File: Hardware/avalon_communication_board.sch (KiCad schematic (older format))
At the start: 22 parts, among them IC1 ENC28J60-I/SO, J1 RJ45_LEDS, P1 B2P-VH, Q1 FMMT597, Q2 BC817, Q3 BC817, Q4 FMMT597, Q5 BC817

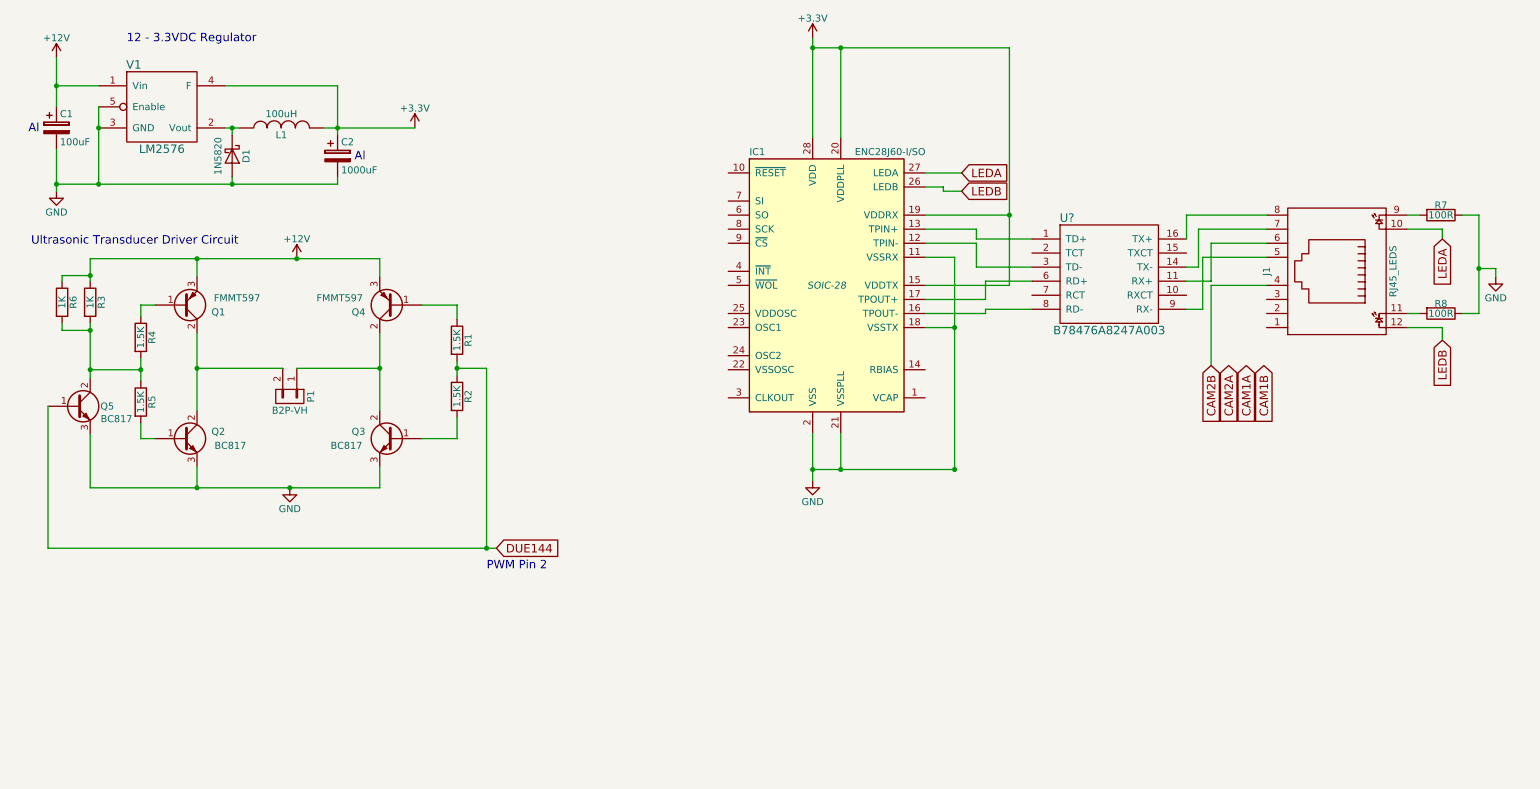
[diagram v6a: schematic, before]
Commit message: -Ethernet Controller Main Schematic Updated
-Main schematic almost complete with Pulse Transformers and Filtering
-Capacitors for Crystal Oscillator need adding
-Ethernet Controller schematic block added to main schematic sheet
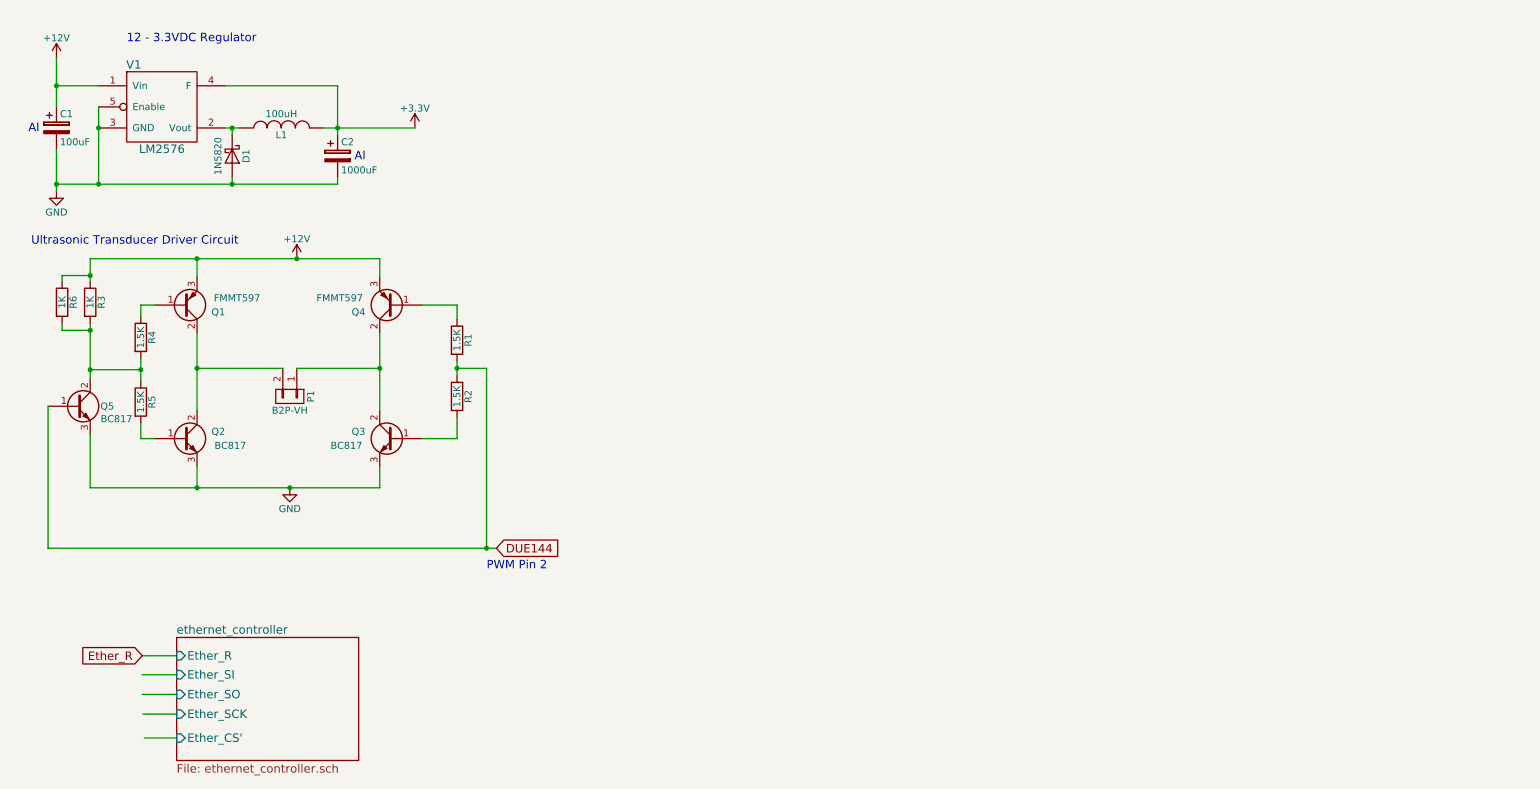
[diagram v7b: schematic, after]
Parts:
- removed IC1: ENC28J60-I/SO, SOIC-28, symbol ENC28J60-I/SO
- removed J1: RJ45_LEDS, symbol RJ45_LEDS
- removed R7, R8: 100R, symbol R
- removed U?: B78476A8247A003, symbol B78476A8247A003
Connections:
- net labels added: Ether_R
- net labels removed: CAM1A, CAM1B, CAM2A, CAM2B, LEDA, LEDB
- wire segments 96 -> 49
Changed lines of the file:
@@
 $Descr A4 11693 8268
 encoding utf-8
-Sheet 1 1
+Sheet 1 2
 Title ""
 Date ""
@@
 $EndComp
 $Comp
-L ENC28J60-I/SO IC1
-U 1 1 5A903E11
-P 6280 2470
-F 0 "IC1" H 5730 3420 50  0000 L CNN
-F 1 "ENC28J60-I/SO" H 6480 3420 50  0000 L CNN
-F 2 "SOIC-28" H 6280 2470 50  0000 C CIN
-F 3 "" H 6280 2470 50  0000 C CNN
-	1    6280 2470
-	1    0    0    -1
-$EndComp
-$Comp
-L RJ45_LEDS J1
-U 1 1 5A9063FA
-P 9910 2370
-F 0 "J1" H 9910 1870 50  0000 C CNN
-F 1 "RJ45_LEDS" H 9910 2770 50  0000 C CNN
-F 2 "" H 9910 2320 50  0000 C CNN
-F 3 "" H 9910 2320 50  0000 C CNN
-	1    9910 2370
-	0    1    -1   0
-$EndComp
-$Comp
 L +12V #PWR4
 U 1 1 5A907F46
@@
 $EndComp
 Connection ~ 2510 2280
-$Comp
-L +3.3V #PWR6
-U 1 1 5A908CDC
-P 6180 710
-F 0 "#PWR6" H 6180 560 50  0001 C CNN
-F 1 "+3.3V" H 6180 850 50  0000 C CNN
-F 2 "" H 6180 710 50  0000 C CNN
-F 3 "" H 6180 710 50  0000 C CNN
-	1    6180 710
-	1    0    0    -1
-$EndComp
-$Comp
-L GND #PWR7
-U 1 1 5A90B1AB
-P 6180 3860
-F 0 "#PWR7" H 6180 3610 50  0001 C CNN
-F 1 "GND" H 6180 3710 50  0000 C CNN
-F 2 "" H 6180 3860 50  0000 C CNN
-F 3 "" H 6180 3860 50  0000 C CNN
-	1    6180 3860
-	1    0    0    -1
-$EndComp
-Text GLabel 7240 1670 2    60   Input ~ 0
-LEDA
-Text GLabel 7240 1800 2    60   Input ~ 0
-LEDB
-$Comp
-L R R7
-U 1 1 5A911D20
-P 10650 1970
-F 0 "R7" V 10580 1970 50  0000 C CNN
-F 1 "100R" V 10650 1970 50  0000 C CNN
-F 2 "" V 10580 1970 50  0000 C CNN
-F 3 "" H 10650 1970 50  0000 C CNN
-	1    10650 1970
-	0    1    1    0
-$EndComp
-$Comp
-L R R8
-U 1 1 5A91211B
-P 10650 2670
-F 0 "R8" V 10580 2670 50  0000 C CNN
-F 1 "100R" V 10650 2670 50  0000 C CNN
-F 2 "" V 10580 2670 50  0000 C CNN
-F 3 "" H 10650 2670 50  0000 C CNN
-	1    10650 2670
-	0    1    1    0
-$EndComp
-Text GLabel 10660 2140 3    60   Input ~ 0
-LEDA
-$Comp
-L GND #PWR9
-U 1 1 5A913778
-P 11040 2410
-F 0 "#PWR9" H 11040 2160 50  0001 C CNN
-F 1 "GND" H 11040 2260 50  0000 C CNN
-F 2 "" H 11040 2410 50  0000 C CNN
-F 3 "" H 11040 2410 50  0000 C CNN
-	1    11040 2410
-	1    0    0    -1
-$EndComp
-Text GLabel 10660 2860 3    60   Input ~ 0
-LEDB
-Wire Wire Line
-	10410 2770 10660 2770
-Wire Wire Line
-	10660 2770 10660 2860
-Wire Wire Line
-	10920 2670 10800 2670
-Wire Wire Line
-	10800 1970 10920 1970
-Wire Wire Line
-	10920 1970 10920 2670
-Wire Wire Line
-	11040 2410 11040 2350
-Wire Wire Line
-	11040 2350 10920 2350
-Connection ~ 10920 2350
-Wire Wire Line
-	10410 2670 10500 2670
-Wire Wire Line
-	10410 1970 10500 1970
-Wire Wire Line
-	10410 2070 10660 2070
-Wire Wire Line
-	10660 2070 10660 2140
-Wire Wire Line
-	6180 780  7580 780
-Wire Wire Line
-	6980 1670 7240 1670
-Wire Wire Line
-	6980 1770 7110 1770
-Wire Wire Line
-	7110 1770 7110 1800
-Wire Wire Line
-	7110 1800 7240 1800
-Wire Wire Line
-	6980 1970 7580 1970
-Wire Wire Line
-	7580 780  7580 2470
-Wire Wire Line
-	6180 710  6180 1420
-Connection ~ 6180 780
-Wire Wire Line
-	6380 1420 6380 780
-Connection ~ 6380 780
-Wire Wire Line
-	7580 2470 6980 2470
-Connection ~ 7580 1970
-Wire Wire Line
-	6180 3520 6180 3860
-Wire Wire Line
-	6380 3520 6380 3780
-Wire Wire Line
-	7190 3780 6180 3780
-Connection ~ 6180 3780
-Wire Wire Line
-	6980 2270 7190 2270
-Wire Wire Line
-	7190 2270 7190 3780
-Wire Wire Line
-	7190 2770 6980 2770
-Connection ~ 7190 2770
-Connection ~ 6380 3780
-Connection ~ 7190 3780
-$Comp
-L B78476A8247A003 U?
-U 1 1 5A907D1C
-P 8290 2290
-F 0 "U?" H 7990 2590 60  0000 C CNN
-F 1 "B78476A8247A003" H 8290 1790 60  0000 C CNN
-F 2 "" H 8290 2290 60  0001 C CNN
-F 3 "" H 8290 2290 60  0001 C CNN
-	1    8290 2290
-	1    0    0    -1
-$EndComp
-Wire Wire Line
-	8840 1970 9410 1970
-Wire Wire Line
-	8925 2070 9410 2070
-Wire Wire Line
-	8925 2070 8925 2340
-Wire Wire Line
-	8840 2440 9015 2440
-Wire Wire Line
-	8955 2270 9410 2270
-Wire Wire Line
-	8925 2340 8840 2340
-Wire Wire Line
-	6980 2070 7345 2070
-Wire Wire Line
-	7345 2070 7345 2140
-Wire Wire Line
-	7345 2140 7740 2140
-Wire Wire Line
-	7345 2340 7740 2340
-Wire Wire Line
-	7345 2340 7345 2170
-Wire Wire Line
-	7345 2170 6980 2170
-Wire Wire Line
-	6980 2570 7410 2570
-Wire Wire Line
-	7410 2570 7410 2440
-Wire Wire Line
-	7410 2440 7740 2440
-Wire Wire Line
-	6980 2670 7410 2670
-Wire Wire Line
-	7410 2670 7410 2640
-Wire Wire Line
-	7410 2640 7740 2640
-Text GLabel 9265 3040 3    60   Input ~ 0
-CAM1A
-Text GLabel 9390 3040 3    60   Input ~ 0
-CAM1B
-Text GLabel 9140 3040 3    60   Input ~ 0
-CAM2A
-Text GLabel 9015 3040 3    60   Input ~ 0
-CAM2B
-Wire Wire Line
-	8955 2640 8840 2640
-Wire Wire Line
-	8955 2270 8955 2640
-Wire Wire Line
-	9015 2470 9015 3040
-Wire Wire Line
-	9015 2440 9015 2170
-Wire Wire Line
-	9015 2170 9410 2170
-Wire Wire Line
-	9015 2470 9410 2470
-Wire Wire Line
-	8840 1970 8840 2140
+$Sheet
+S 1655 4975 1295 875
+U 5A91950F
+F0 "ethernet_controller" 60
+F1 "ethernet_controller.sch" 60
+F2 "Ether_R" I L 1655 5105 60
+F3 "Ether_SI" I L 1655 5240 60
+F4 "Ether_SO" I L 1655 5380 60
+F5 "Ether_SCK" I L 1655 5520 60
+F6 "Ether_CS'" I L 1655 5690 60
+$EndSheet
+Wire Wire Line
+	1655 5105 1410 5105
+Wire Wire Line
+	1655 5240 1410 5240
+Wire Wire Line
+	1655 5380 1410 5380
+Wire Wire Line
+	1655 5520 1415 5520
+Wire Wire Line
+	1655 5690 1425 5690
+Text GLabel 1410 5105 0    60   Input ~ 0
+Ether_R
 $EndSCHEMATC

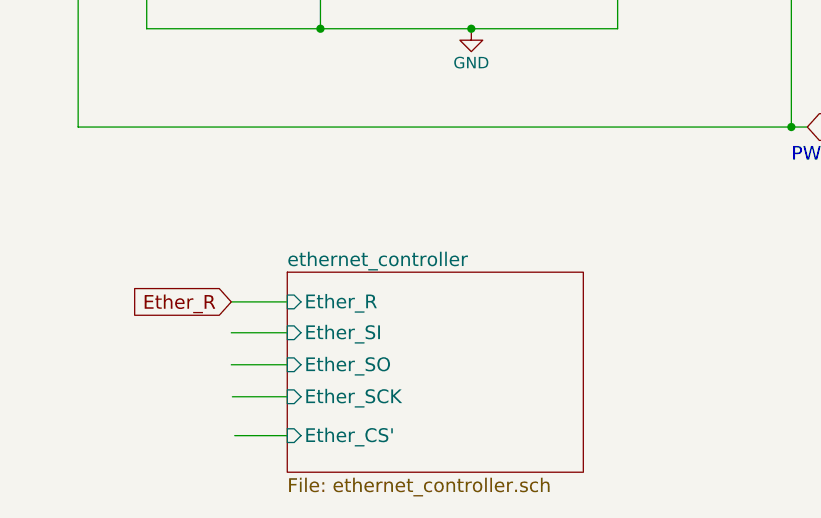
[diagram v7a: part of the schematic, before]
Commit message: -Continued work on the Ethernet Controller Schematic
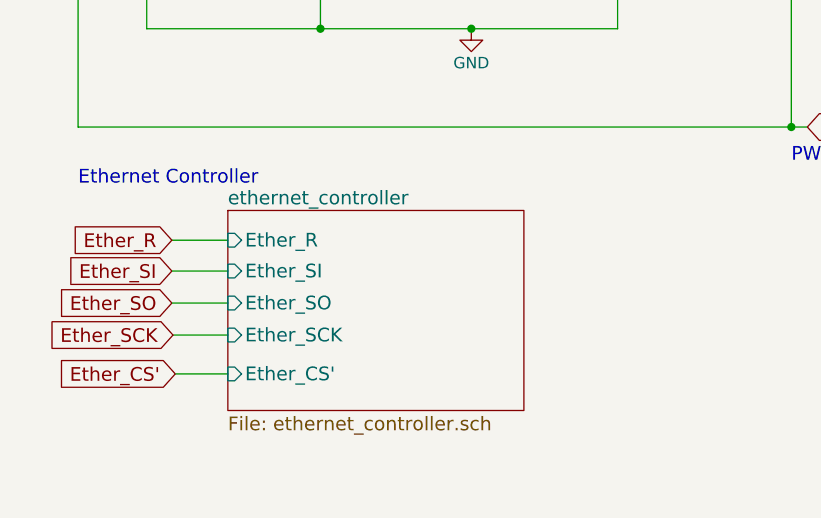
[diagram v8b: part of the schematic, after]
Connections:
- net labels added: Ether_CS', Ether_SCK, Ether_SI, Ether_SO
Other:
- note added: "Ethernet Controller"
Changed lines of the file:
@@
 EESchema Schematic File Version 2
+LIBS:avalon_communication_board-rescue
 LIBS:power
 LIBS:device
@@
 Connection ~ 2510 2280
 $Sheet
-S 1655 4975 1295 875
+S 1395 4705 1295 875
 U 5A91950F
 F0 "ethernet_controller" 60
 F1 "ethernet_controller.sch" 60
-F2 "Ether_R" I L 1655 5105 60
-F3 "Ether_SI" I L 1655 5240 60
-F4 "Ether_SO" I L 1655 5380 60
-F5 "Ether_SCK" I L 1655 5520 60
-F6 "Ether_CS'" I L 1655 5690 60
+F2 "Ether_R" I L 1395 4835 60
+F3 "Ether_SI" I L 1395 4970 60
+F4 "Ether_SO" I L 1395 5110 60
+F5 "Ether_SCK" I L 1395 5250 60
+F6 "Ether_CS'" I L 1395 5420 60
 $EndSheet
 Wire Wire Line
-	1655 5105 1410 5105
-Wire Wire Line
-	1655 5240 1410 5240
-Wire Wire Line
-	1655 5380 1410 5380
-Wire Wire Line
-	1655 5520 1415 5520
-Wire Wire Line
-	1655 5690 1425 5690
-Text GLabel 1410 5105 0    60   Input ~ 0
+	1395 4835 1150 4835
+Wire Wire Line
+	1395 4970 1150 4970
+Wire Wire Line
+	1395 5110 1150 5110
+Wire Wire Line
+	1395 5250 1155 5250
+Wire Wire Line
+	1395 5420 1165 5420
+Text GLabel 1150 4835 0    60   Input ~ 0
 Ether_R
+Text Notes 740  4600 0    60   ~ 0
+Ethernet Controller
+Text GLabel 1150 4970 0    60   Input ~ 0
+Ether_SI
+Text GLabel 1150 5110 0    60   Input ~ 0
+Ether_SO
+Text GLabel 1155 5250 0    60   Input ~ 0
+Ether_SCK
+Text GLabel 1165 5420 0    60   Input ~ 0
+Ether_CS'
 $EndSCHEMATC
